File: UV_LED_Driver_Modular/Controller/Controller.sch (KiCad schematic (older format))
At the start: 1 part, among them J3 Conn_02x06_Odd_Even

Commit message: Changed TO225 NPN (MJE340) to SOT223 NPN (PZT2222A)
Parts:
- added Q1, Q2: Q_NPN_ECB, Package_TO_SOT_THT:TO-220-3_Vertical, symbol Device:Q_NPN_ECB
- added R1, R2: 1K, Resistor_SMD:R_1206_3216Metric_Pad1.42x1.75mm_HandSolder, symbol Device:R
- added R3, R4: 2K2, Resistor_SMD:R_1206_3216Metric_Pad1.42x1.75mm_HandSolder, symbol Device:R
- J3: footprint (none) -> Connector_IDC:IDC-Header_2x06_P2.54mm_Vertical
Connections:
- net labels added: +3.3V
- wire segments 28 -> 42
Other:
- note removed: "NOT CONNECTED"

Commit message: updated
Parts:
- removed Q1, Q2: Q_NPN_ECB, Package_TO_SOT_THT:TO-220-3_Vertical, symbol Device:Q_NPN_ECB
- added J4: Conn_01x03, Connector_Molex:Molex_KK-254_AE-6410-03A_1x03_P2.54mm_Vertical, symbol Connector_Generic:Conn_01x03
- added Q1, Q2, Q3: Q_NPN_BCE, Package_TO_SOT_SMD:SOT-223-3_TabPin2, symbol Device:Q_NPN_BCE
- added R5: 1K, Resistor_SMD:R_1206_3216Metric_Pad1.42x1.75mm_HandSolder, symbol Device:R
- added R6: 2K2, Resistor_SMD:R_1206_3216Metric_Pad1.42x1.75mm_HandSolder, symbol Device:R
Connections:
- net labels added: LED_PWM_OUT, STATUS_PWM_OUT, UV_PWM_OUT
- net labels removed: LED_PWM, UV_PWM
- wire segments 42 -> 54
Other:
- moved on the sheet: J3, R1, R2, R3, R4

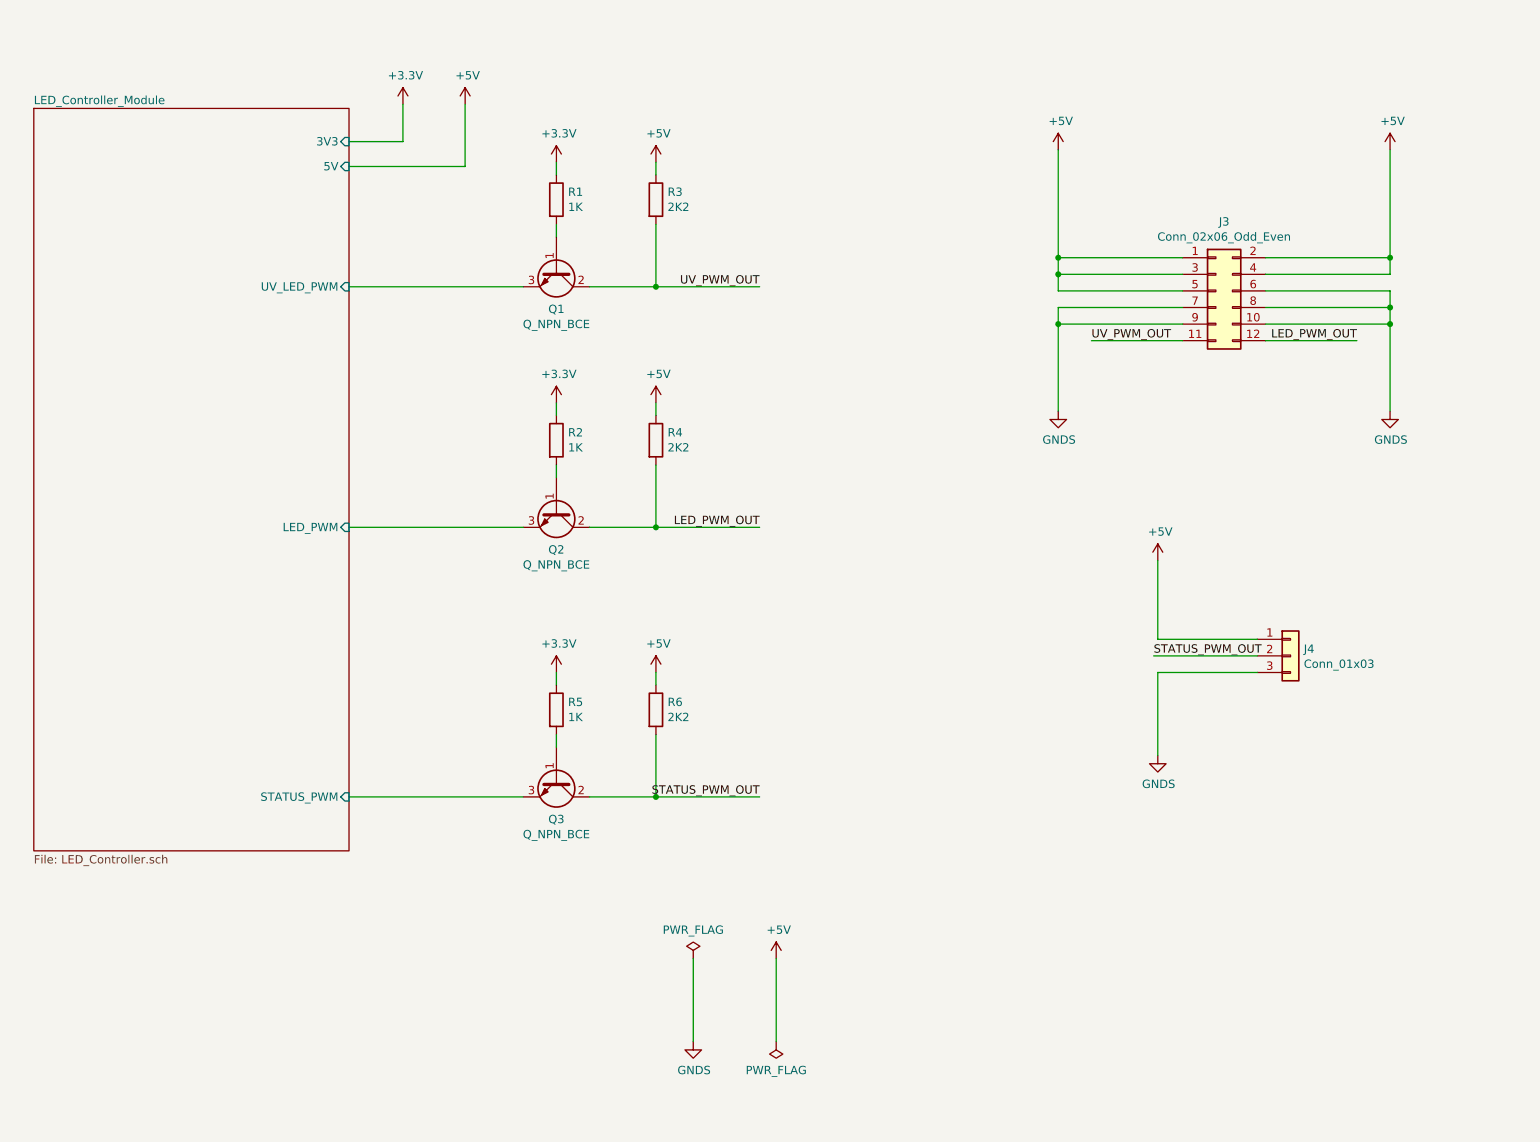
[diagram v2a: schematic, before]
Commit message: added IRS4427 mosfet gate driver to controller design
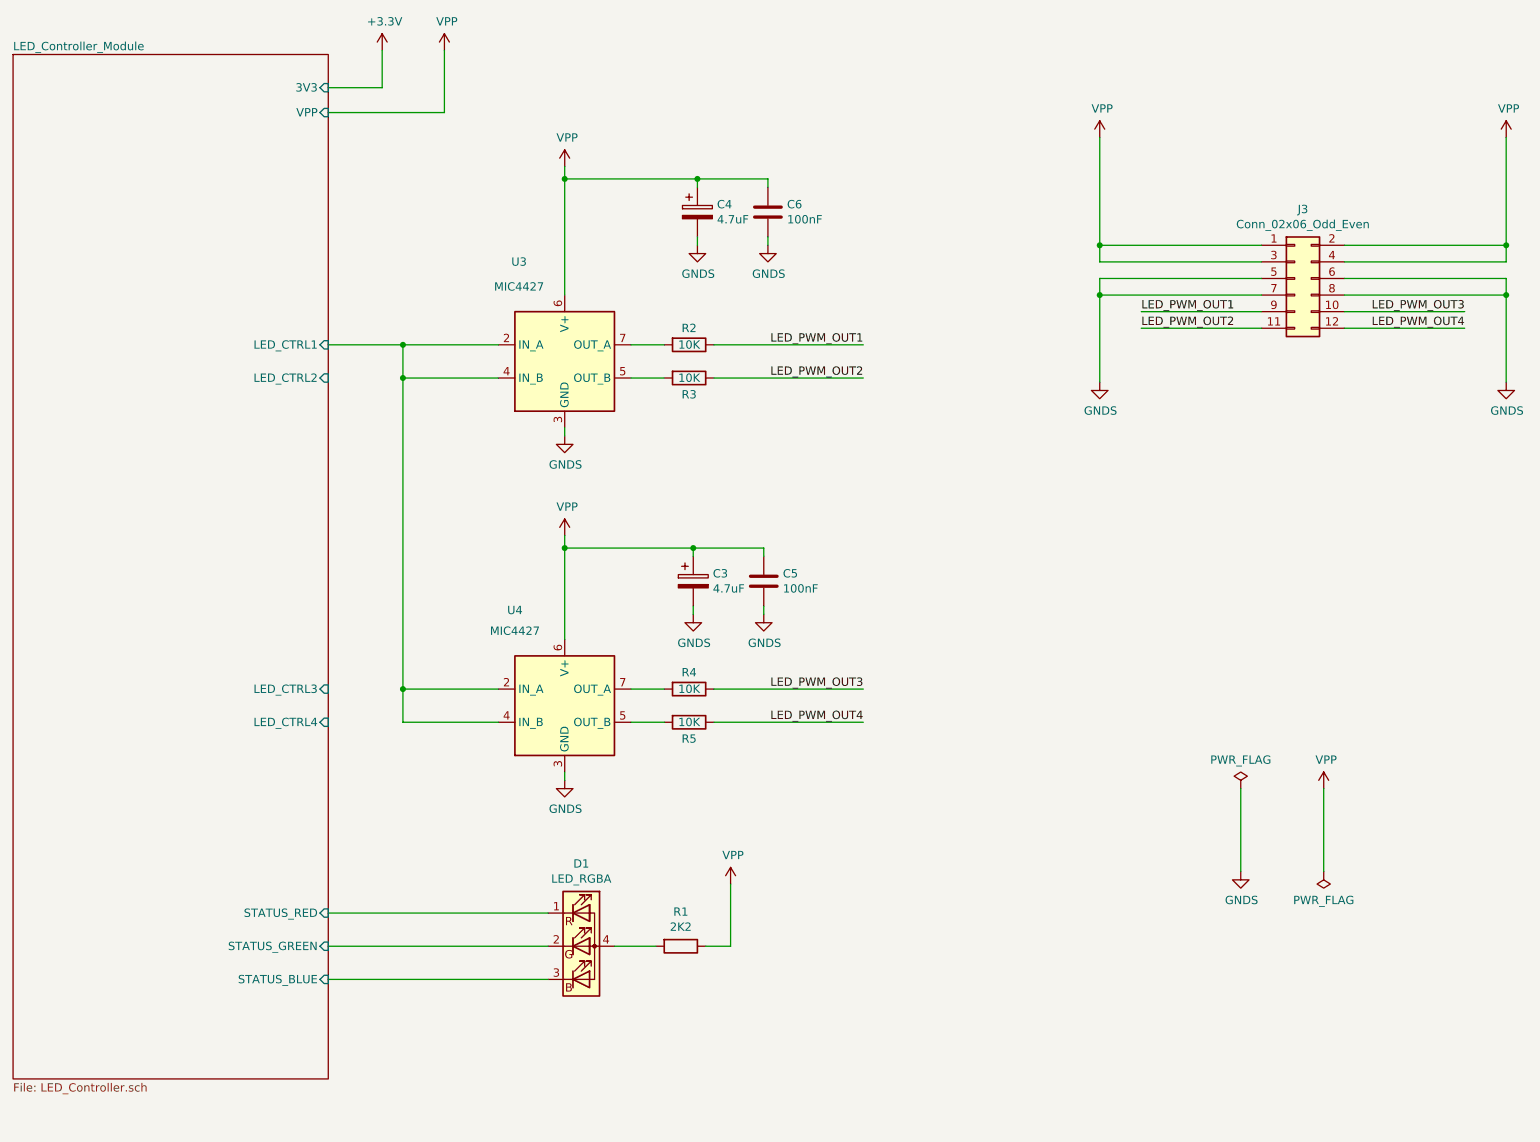
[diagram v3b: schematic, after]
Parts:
- removed J4: Conn_01x03, Connector_Molex:Molex_KK-254_AE-6410-03A_1x03_P2.54mm_Vertical, symbol Connector_Generic:Conn_01x03
- removed Q1, Q2, Q3: Q_NPN_BCE, Package_TO_SOT_SMD:SOT-223-3_TabPin2, symbol Device:Q_NPN_BCE
- removed R6: 2K2, Resistor_SMD:R_1206_3216Metric_Pad1.42x1.75mm_HandSolder, symbol Device:R
- added C3, C4: 4.7uF, symbol Device:CP
- added C5, C6: 100nF, symbol Device:C
- added D1: LED_RGBA, symbol Device:LED_RGBA
- added U3, U4: MIC4427, symbol Driver_FET:MIC4427
- R1: value 1K -> 2K2; footprint Resistor_SMD:R_1206_3216Metric_Pad1.42x1.75mm_HandSolder -> (none)
- R2, R5: value 1K -> 10K; footprint Resistor_SMD:R_1206_3216Metric_Pad1.42x1.75mm_HandSolder -> (none)
- R3, R4: value 2K2 -> 10K; footprint Resistor_SMD:R_1206_3216Metric_Pad1.42x1.75mm_HandSolder -> (none)
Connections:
- net +3V3: no longer R1.1, R2.1, R5.1
- net GNDS: now also J3.5 (Pin_5), C3.2, C4.2, C5.2, C6.2, U3.3 (GND), U4.3 (GND); no longer J3.10 (Pin_10), J3.9 (Pin_9)
- net at R1.2: now also D1.4 (A)
- net at R2.2: now also U3.7 (OUT_A)
- net at R5.2: now also U4.5 (OUT_B)
- net +5V renamed VPP
- net VPP: now also R1.1, C3.1, C4.1, C5.1, C6.1, U3.6 (V+), U4.6 (V+); no longer J3.5 (Pin_5), R3.1, R4.1
- net LED_PWM_OUT: no longer names the net of R4.2
- net LED_PWM_OUT: now also U4.7 (OUT_A); no longer J3.12 (Pin_12)
- net UV_PWM_OUT: no longer names the net of R3.2
- net UV_PWM_OUT: now also U3.5 (OUT_B); no longer J3.11 (Pin_11)
- new net LED_Controller_Module/LED_CTRL1: U3.2 (IN_A), U3.4 (IN_B), U4.2 (IN_A), U4.4 (IN_B)
- new net LED_Controller_Module/STATUS_BLUE: D1.3 (BK)
- new net LED_Controller_Module/STATUS_GREEN: D1.2 (GK)
- new net LED_Controller_Module/STATUS_RED: D1.1 (RK)
- new net LED_PWM_OUT1: J3.9 (Pin_9), R2.1
- new net LED_PWM_OUT2: J3.11 (Pin_11), R3.1
- new net LED_PWM_OUT3: J3.10 (Pin_10), R4.1
- new net LED_PWM_OUT4: J3.12 (Pin_12), R5.1
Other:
- moved on the sheet: J3

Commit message: docs update
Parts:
- removed C3, C4: 4.7uF, symbol Device:CP
- removed C5, C6: 100nF, symbol Device:C
- removed J3: Conn_02x06_Odd_Even, Connector_IDC:IDC-Header_2x06_P2.54mm_Vertical, symbol Connector_Generic:Conn_02x06_Odd_Even
- removed R2, R3, R4, R5: 10K, symbol Device:R
- removed U3, U4: MIC4427, symbol Driver_FET:MIC4427
- added J3: Conn_02x08_Odd_Even, Connector_PinHeader_2.54mm:PinHeader_2x08_P2.54mm_Vertical, symbol Connector_Generic:Conn_02x08_Odd_Even
- D1: footprint (none) -> Connector_PinHeader_2.54mm:PinHeader_1x04_P2.54mm_Vertical
- R1: footprint (none) -> Resistor_SMD:R_1206_3216Metric_Pad1.42x1.75mm_HandSolder
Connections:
- net GNDS: now also J3.12 (Pin_12), J3.13 (Pin_13), J3.14 (Pin_14), J3.15 (Pin_15), J3.16 (Pin_16)
- net LED_PWM_OUT1: now also J3.3 (Pin_3)
- net LED_PWM_OUT2: now also J3.1 (Pin_1)
- net LED_PWM_OUT3: now also J3.2 (Pin_2)
- net LED_PWM_OUT4: now also J3.4 (Pin_4)
- net VPP: now also J3.10 (Pin_10), J3.11 (Pin_11), J3.7 (Pin_7), J3.8 (Pin_8), J3.9 (Pin_9)
- new net LED_PWM_OUT5: J3.6 (Pin_6)
- no-connect marks 0 -> 1
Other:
- moved on the sheet: D1, R1
